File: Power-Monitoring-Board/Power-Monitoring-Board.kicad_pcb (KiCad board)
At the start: 2 copper layers, 25 parts, among them J1 Conn_01x02_Pin, U1 NUCLEO_L432KC, U2 ST7735R, U3 INA260AIPWR, U4 TPS562231DRLR

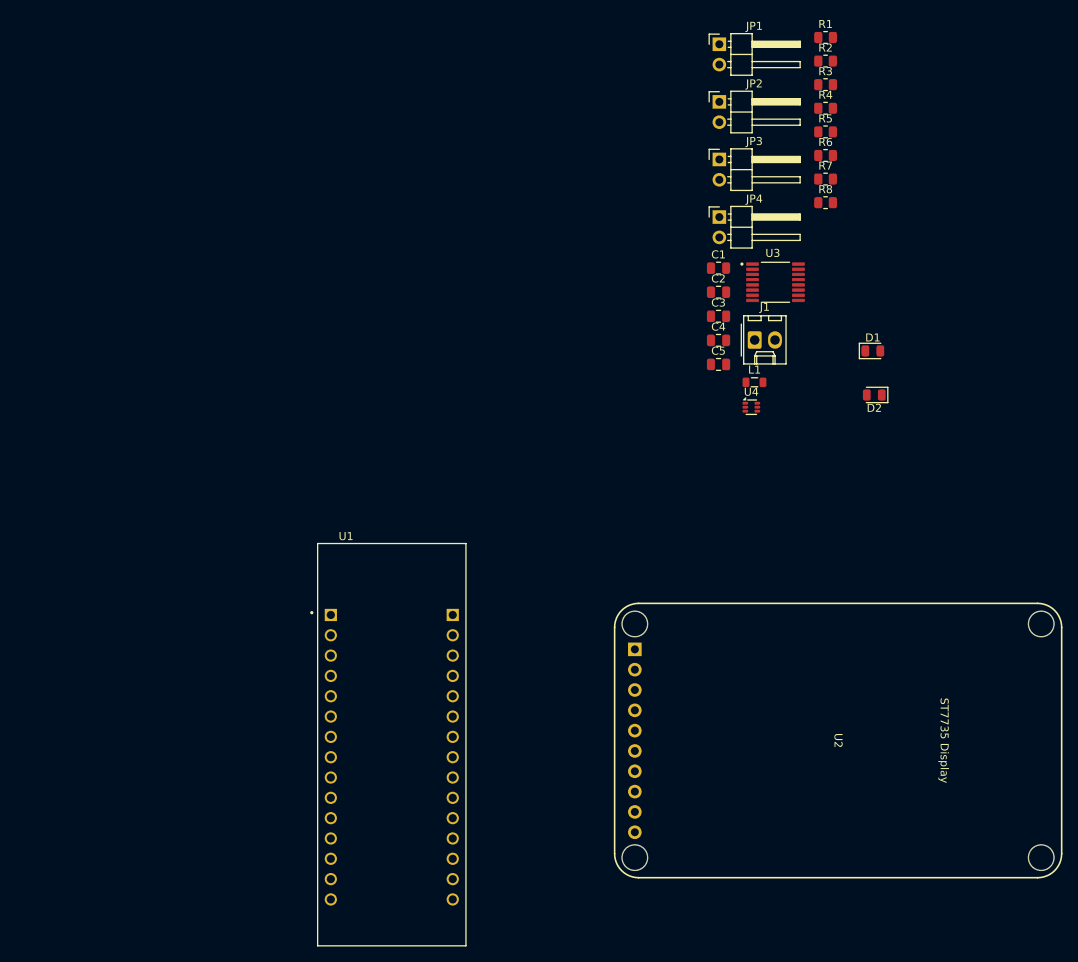
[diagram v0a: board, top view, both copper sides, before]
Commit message: update sch and footprints
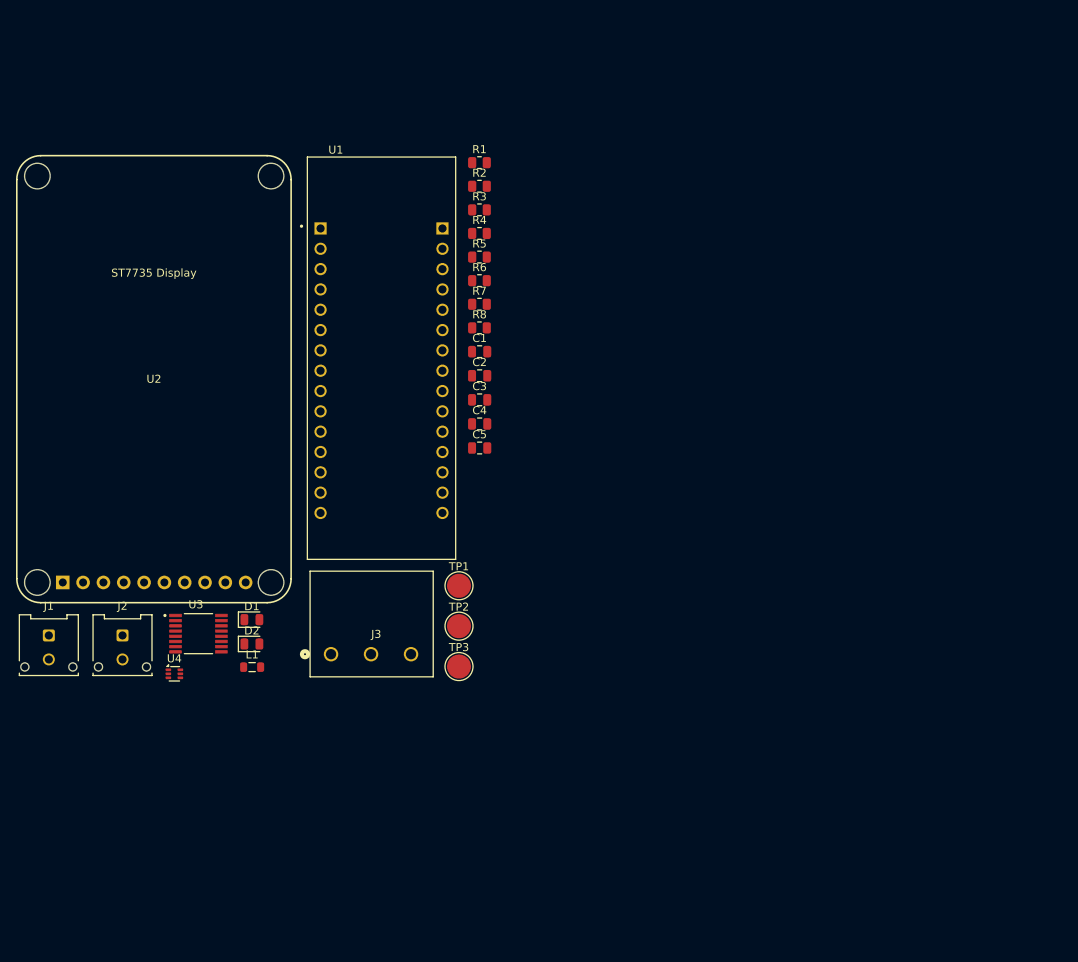
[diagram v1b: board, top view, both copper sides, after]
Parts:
- removed JP1, JP2, JP3, JP4: Jumper_2_Bridged, Connector_PinHeader_2.54mm:PinHeader_1x02_P2.54mm_Horizontal
- added J2: Conn_01x02_Pin, Connector_Molex:Molex_Micro-Fit_3.0_43045-0212_2x01_P3.00mm_Vertical, F.Cu at (89.2, 117.8)
- added J3: Conn_01x03_Pin, Power-Monitoring:CONN_1988817, F.Cu at (125.4, 120.2)
- added TP1: TestPoint, TestPoint:TestPoint_Pad_D3.0mm, F.Cu at (131.3, 111.6)
- added TP2: TestPoint, TestPoint:TestPoint_Pad_D3.0mm, F.Cu at (131.3, 116.7)
- added TP3: TestPoint, TestPoint:TestPoint_Pad_D3.0mm, F.Cu at (131.3, 121.7)
- J1: footprint Connector_Molex:Molex_KK-254_AE-6410-02A_1x02_P2.54mm_Vertical -> Connector_Molex:Molex_Micro-Fit_3.0_43045-0212_2x01_P3.00mm_Vertical
- moved U2 96.7 mm to (93.1, 85.8), turned to 0 degrees
- moved J1 95.6 mm to (80.0, 117.8)
- moved D1 84.6 mm to (105.4, 115.8)
- moved U3 84.4 mm to (98.7, 117.6)
- moved D2 83.8 mm to (105.4, 118.9), turned to 0 degrees
- moved U4 79.4 mm to (95.7, 122.6)
- moved L1 72.2 mm to (105.4, 121.8)
- moved U1 48.3 mm to (121.6, 83.2)
- moved R1 46.0 mm to (133.8, 58.7)
- moved R2 46.0 mm to (133.8, 61.7)
- moved R3 46.0 mm to (133.8, 64.6)
- moved R4 46.0 mm to (133.8, 67.6)
- moved R5 46.0 mm to (133.8, 70.5)
- moved R6 46.0 mm to (133.8, 73.5)
- moved R7 46.0 mm to (133.8, 76.4)
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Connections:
- J1 pad 2: /V- -> GND
- U3 pad 5: Net-(JP1-A) -> GND
